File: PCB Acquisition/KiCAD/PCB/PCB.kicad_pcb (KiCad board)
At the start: 2 copper layers, 1 part, among them U1 PIC24F32KA302-I_SS

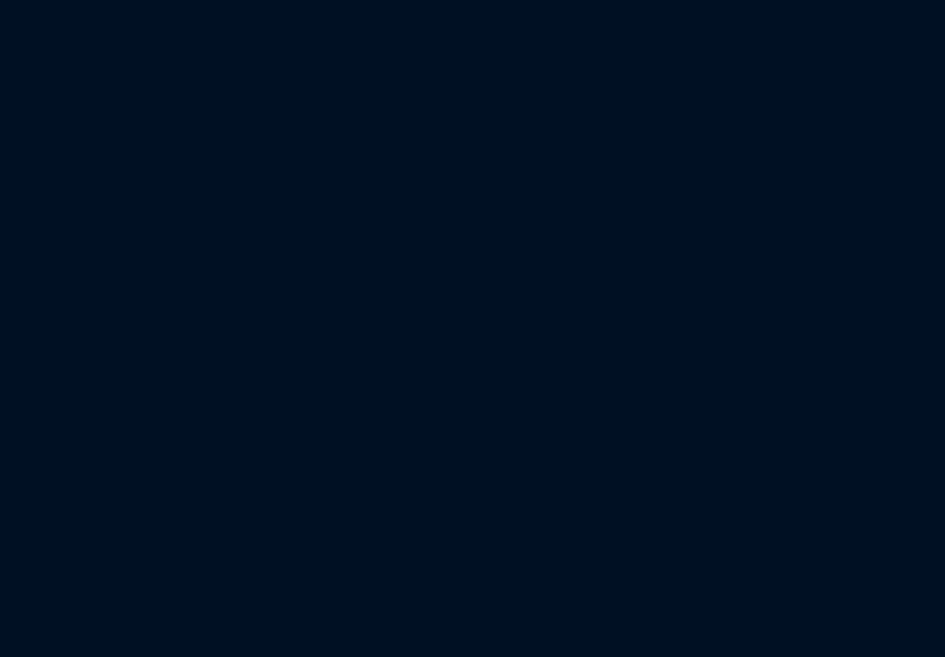
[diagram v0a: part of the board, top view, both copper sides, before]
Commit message: Début du layout
Les pièces ont été choisies pour le PCB et le layout du PCB avec celles-ci est commencé. Il reste à finaliser le layout.
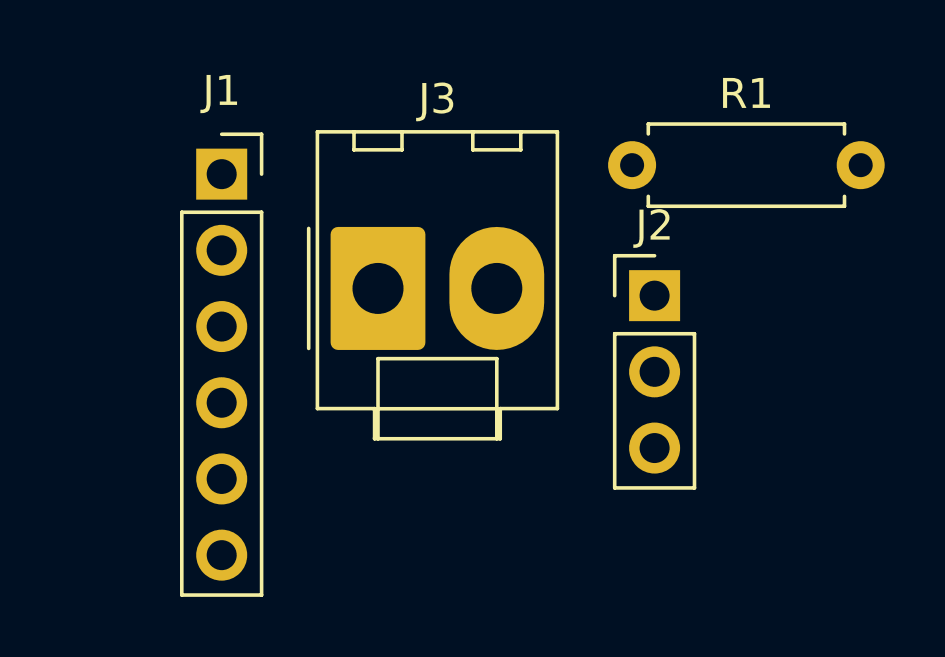
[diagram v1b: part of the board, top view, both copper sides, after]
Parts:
- added J1: Conn_01x06_Female, Connector_PinSocket_2.54mm:PinSocket_1x06_P2.54mm_Vertical, F.Cu at (178.4, 84.4)
- added J2: Conn_01x03_Male, Connector_PinHeader_2.54mm:PinHeader_1x03_P2.54mm_Vertical, F.Cu at (192.8, 88.4)
- added J3: Conn_01x02_Male, Connector_Molex:Molex_KK-396_A-41791-0002_1x02_P3.96mm_Vertical, F.Cu at (183.6, 88.2)
- added R1: 1k, Resistor_THT:R_Axial_DIN0207_L6.3mm_D2.5mm_P7.62mm_Horizontal, F.Cu at (192.0, 84.1)

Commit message: PCB Layout
Layout du PCB
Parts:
- moved J2 45.6 mm to (147.3, 91.4)
- moved J1 41.3 mm to (137.2, 81.3)
- moved R1 41.0 mm to (151.1, 81.5), turned to 180 degrees
- moved J3 7.75 mm to (176.5, 91.4), turned to 90 degrees
- moved U1 2.84 mm to (162.6, 87.6)
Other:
- board outline added: 61 x 25.4 mm
- net class Default: clearance 0.2 -> 0.254; trace_width 0.25 -> 0.254; via_dia 0.8 -> 0.762; via_drill 0.4 -> 0.381
- rule pad_to_mask_clearance: 0.051 -> 0.0508
- rule trace_clearance: 0.2 -> 0.254
- rule trace_min: 0.2 -> 0.1524
- rule via_min_drill: 0.3 -> 0.3302
- rule via_min_size: 0.4 -> 0.6858
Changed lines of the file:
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@@
   (general
     (thickness 1.6)
-    (drawings 0)
+    (drawings 4)
     (tracks 0)
     (zones 0)
@@
   )
   (setup
-    (last_trace_width 0.25)
-    (trace_clearance 0.2)
+    (last_trace_width 0.254)
+    (trace_clearance 0.254)
     (zone_clearance 0.508)
     (zone_45_only no)
-    (trace_min 0.2)
-    (via_size 0.8)
-    (via_drill 0.4)
-    (via_min_size 0.4)
-    (via_min_drill 0.3)
-    (uvia_size 0.3)
-    (uvia_drill 0.1)
+    (trace_min 0.1524)
+    (via_size 0.762)
+    (via_drill 0.381)
+    (via_min_size 0.6858)
+    (via_min_drill 0.3302)
+    (uvia_size 0.762)
+    (uvia_drill 0.381)
     (uvias_allowed no)
-    (uvia_min_size 0.2)
-    (uvia_min_drill 0.1)
+    (uvia_min_size 0.6858)
+    (uvia_min_drill 0.3302)
     (edge_width 0.05)
     (segment_width 0.2)
@@
     (pad_size 1.524 1.524)
     (pad_drill 0.762)
-    (pad_to_mask_clearance 0.051)
+    (pad_to_mask_clearance 0.0508)
     (solder_mask_min_width 0.25)
     (aux_axis_origin 0 0)
@@
   (net 29 "Net-(J3-Pad2)")
   (net_class Default "This is the default net class."
-    (clearance 0.2)
-    (trace_width 0.25)
-    (via_dia 0.8)
-    (via_drill 0.4)
-    (uvia_dia 0.3)
-    (uvia_drill 0.1)
+    (clearance 0.254)
+    (trace_width 0.254)
+    (via_dia 0.762)
+    (via_drill 0.381)
+    (uvia_dia 0.762)
+    (uvia_drill 0.381)
     (add_net "Net-(J1-Pad1)")
     (add_net "Net-(J1-Pad2)")
@@
   )
   (module 24FV32KA302A:PIC24F32KA302-I&slash_SS (layer F.Cu)
-    (at 161.29 90.17)
+    (at 162.56 87.63)
     (fp_text reference U1 (at 0 0) (layer F.SilkS)
       (effects (font (size 1 1) (thickness 0.15)))
@@
   )
   (module Connector_PinSocket_2.54mm:PinSocket_1x06_P2.54mm_Vertical (layer F.Cu)
-    (at 178.355001 84.375001)
+    (at 137.16 81.28)
     (descr "Through hole straight socket strip, 1x06, 2.54mm pitch, single row (from Kicad 4.0.7), script generated")
     (tags "Through hole socket strip THT 1x06 2.54mm single row")
@@
   )
   (module Connector_PinHeader_2.54mm:PinHeader_1x03_P2.54mm_Vertical (layer F.Cu)
-    (at 192.785001 88.425001)
+    (at 147.32 91.44)
     (descr "Through hole straight pin header, 1x03, 2.54mm pitch, single row")
     (tags "Through hole pin header THT 1x03 2.54mm single row")
@@
   )
   (module Connector_Molex:Molex_KK-396_A-41791-0002_1x02_P3.96mm_Vertical (layer F.Cu)
-    (at 183.565001 88.185001)
+    (at 176.53 91.44 90)
     (descr "Molex KK 396 Interconnect System, old/engineering part number: A-41791-0002 example for new part number: 26-60-4020, 2 Pins (https://www.molex.com/pdm_docs/sd/026604020_sd.pdf), generated with kicad-footprint-generator")
     (tags "connector Molex KK-396 vertical")
-    (fp_text reference J3 (at 1.98 -6.31) (layer F.SilkS)
-      (effects (font (size 1 1) (thickness 0.15)))
-    )
-    (fp_text value Conn_01x02_Male (at 1.98 6.1) (layer F.Fab)
+    (fp_text reference J3 (at 1.98 -6.31 90) (layer F.SilkS)
+      (effects (font (size 1 1) (thickness 0.15)))
+    )
+    (fp_text value Conn_01x02_Male (at 1.98 6.1 90) (layer F.Fab)
       (effects (font (size 1 1) (thickness 0.15)))
     )
@@
     (fp_line (start 6.37 5.4) (end 6.37 -5.61) (layer F.CrtYd) (width 0.05))
     (fp_line (start 6.37 -5.61) (end -2.41 -5.61) (layer F.CrtYd) (width 0.05))
-    (fp_text user %R (at 1.98 -4.41) (layer F.Fab)
-      (effects (font (size 1 1) (thickness 0.15)))
-    )
-    (pad 1 thru_hole roundrect (at 0 0) (size 3.16 4.1) (drill 1.7) (layers *.Cu *.Mask) (roundrect_rratio 0.079114)
+    (fp_text user %R (at 1.98 -4.41 90) (layer F.Fab)
+      (effects (font (size 1 1) (thickness 0.15)))
+    )
+    (pad 1 thru_hole roundrect (at 0 0 90) (size 3.16 4.1) (drill 1.7) (layers *.Cu *.Mask) (roundrect_rratio 0.079114)
       (net 28 "Net-(J3-Pad1)"))
-    (pad 2 thru_hole oval (at 3.96 0) (size 3.16 4.1) (drill 1.7) (layers *.Cu *.Mask)
+    (pad 2 thru_hole oval (at 3.96 0 90) (size 3.16 4.1) (drill 1.7) (layers *.Cu *.Mask)
       (net 29 "Net-(J3-Pad2)"))
     (model ${KISYS3DMOD}/Connector_Molex.3dshapes/Molex_KK-396_A-41791-0002_1x02_P3.96mm_Vertical.wrl
@@
   )
   (module Resistor_THT:R_Axial_DIN0207_L6.3mm_D2.5mm_P7.62mm_Horizontal (layer F.Cu)
-    (at 192.035001 84.075001)
+    (at 151.13 81.535001 180)
     (descr "Resistor, Axial_DIN0207 series, Axial, Horizontal, pin pitch=7.62mm, 0.25W = 1/4W, length*diameter=6.3*2.5mm^2, http://cdn-reichelt.de/documents/datenblatt/B400/1_4W%23YAG.pdf")
     (tags "Resistor Axial_DIN0207 series Axial Horizontal pin pitch 7.62mm 0.25W = 1/4W length 6.3mm diameter 2.5mm")
@@
       (effects (font (size 1 1) (thickness 0.15)))
     )
-    (pad 1 thru_hole circle (at 0 0) (size 1.6 1.6) (drill 0.8) (layers *.Cu *.Mask)
+    (pad 1 thru_hole circle (at 0 0 180) (size 1.6 1.6) (drill 0.8) (layers *.Cu *.Mask)
       (net 21 "Net-(J1-Pad1)"))
-    (pad 2 thru_hole oval (at 7.62 0) (size 1.6 1.6) (drill 0.8) (layers *.Cu *.Mask)
+    (pad 2 thru_hole oval (at 7.62 0 180) (size 1.6 1.6) (drill 0.8) (layers *.Cu *.Mask)
       (net 22 "Net-(J1-Pad2)"))
     (model ${KISYS3DMOD}/Resistor_THT.3dshapes/R_Axial_DIN0207_L6.3mm_D2.5mm_P7.62mm_Horizontal.wrl
@@
     )
   )
+  (gr_line (start 127 101.6) (end 187.96 101.6) (layer Edge.Cuts) (width 0.0254))
+  (gr_line (start 187.96 76.2) (end 187.96 101.6) (layer Edge.Cuts) (width 0.0254))
+  (gr_line (start 127 76.2) (end 187.96 76.2) (layer Edge.Cuts) (width 0.0254))
+  (gr_line (start 127 101.6) (end 127 76.2) (layer Edge.Cuts) (width 0.0254))
 )

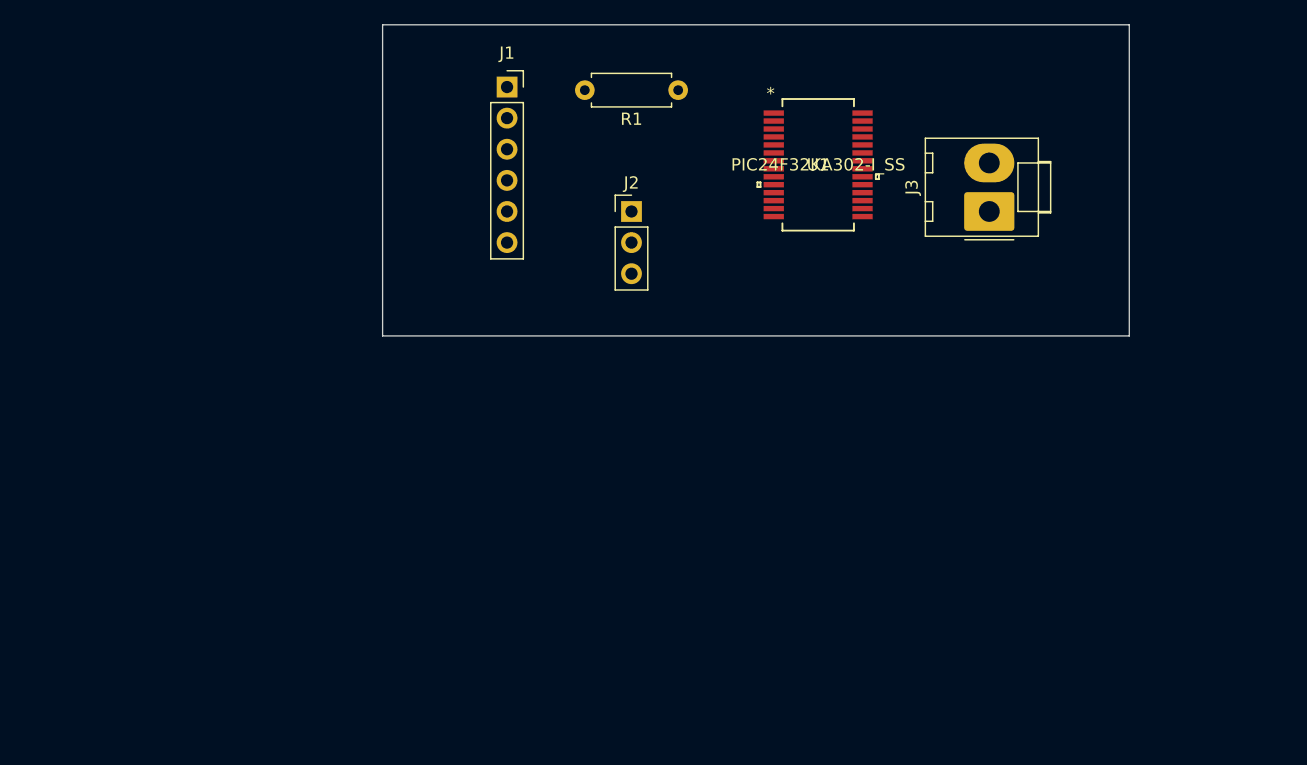
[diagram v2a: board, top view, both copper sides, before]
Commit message: Poursuite du layout (tracks)
Les tracks sont finies.
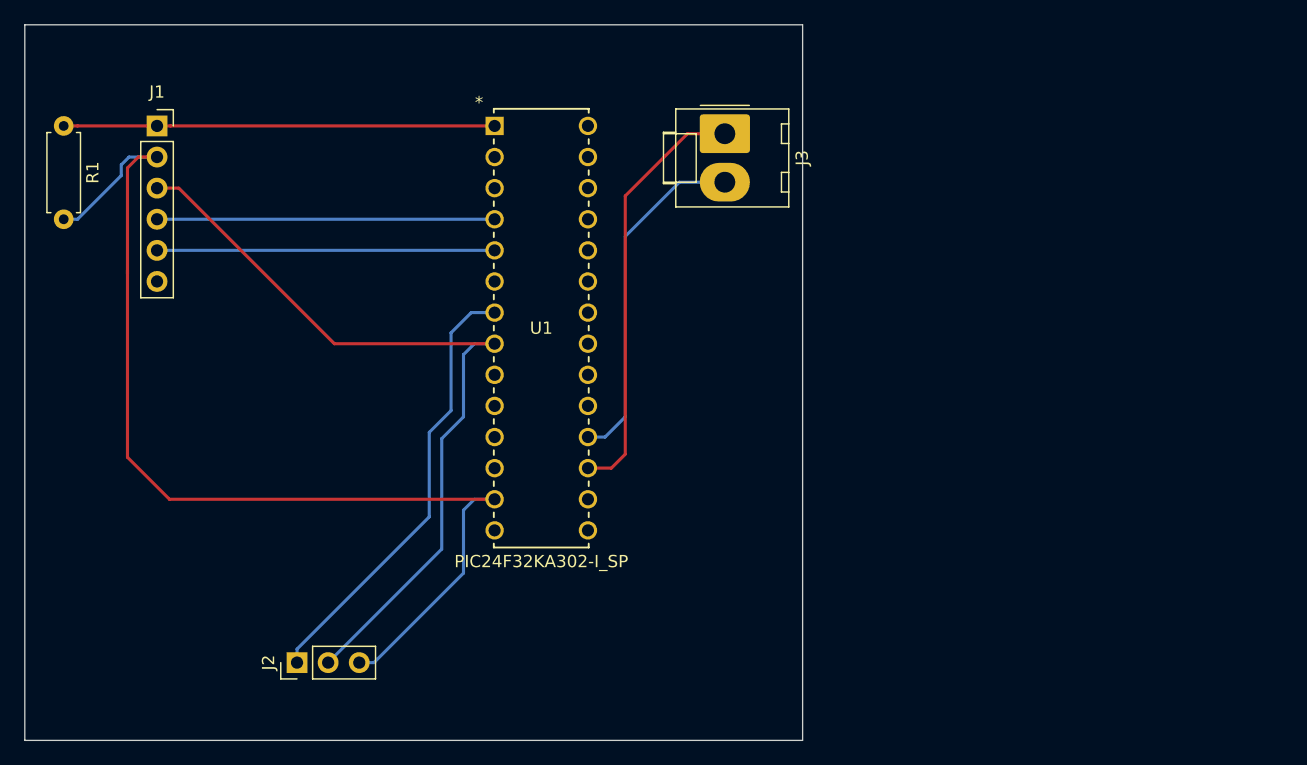
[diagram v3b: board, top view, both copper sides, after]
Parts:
- U1: value PIC24F32KA302-I_SS -> PIC24F32KA302-I_SP; footprint 24FV32KA302A:PIC24F32KA302-I&slash_SS -> PIC24F32KA302:PIC24F32KA302-I&slash_SP
- moved R1 50.2 mm to (101.0, 84.5), turned to 270 degrees
- moved J2 45.8 mm to (120.0, 128.3), turned to 90 degrees
- moved J1 28.8 mm to (108.6, 84.5)
- moved U1 26.6 mm to (136.1, 84.5)
- moved J3 22.5 mm to (154.9, 85.1), turned to 270 degrees
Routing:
- net Net-(J1-Pad2): track 0.00 -> 87.9 mm
- net Net-(J1-Pad3): track 0.00 -> 65.5 mm
- net Net-(J2-Pad1): track 0.00 -> 36.4 mm
- net Net-(J1-Pad1): track 0.00 -> 35.2 mm
- net Net-(J3-Pad1): track 0.00 -> 34.8 mm
- net Net-(J3-Pad2): track 0.00 -> 28.4 mm
- net Net-(J1-Pad5): track 0.00 -> 27.6 mm
- net Net-(J1-Pad4): track 0.00 -> 27.6 mm
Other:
- board size 61 x 25.4 mm -> 63.5 x 58.4 mm

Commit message: PCB fini
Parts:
- removed U1: PIC24F32KA302-I_SP, PIC24F32KA302:PIC24F32KA302-I&slash_SP
- added J4: Conn_01x02_Male, Connector_Molex:Molex_KK-396_A-41791-0002_1x02_P3.96mm_Vertical, F.Cu at (154.9, 97.8)
- J1: value Conn_01x06_Female -> Conn_01x05_Female; footprint Connector_PinSocket_2.54mm:PinSocket_1x06_P2.54mm_Vertical -> Connector_PinSocket_2.54mm:PinSocket_1x05_P2.54mm_Vertical
- J3: value Conn_01x02_Male -> ED281DT; footprint Connector_Molex:Molex_KK-396_A-41791-0002_1x02_P3.96mm_Vertical -> digikey-footprints:Socket_DIP-28_7.62mm_Conn
- moved J3 15.4 mm to (139.6, 84.5), turned to 0 degrees
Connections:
- J3 pad 1: Net-(J3-Pad1) -> Net-(J1-Pad1)
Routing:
- net Net-(J3-Pad1): track 34.8 -> 0.00 mm
- net Net-(J3-Pad2): track 28.4 -> 0.00 mm
- net Net-(J3-Pad18): track 0.00 -> 19.4 mm
- net Net-(J3-Pad17): track 0.00 -> 15.4 mm
- net Net-(J1-Pad2): track 87.9 -> 95.4 mm
- net Net-(J1-Pad3): track 65.5 -> 70.4 mm
- net Net-(J1-Pad5): track 27.6 -> 31.0 mm
- net Net-(J1-Pad4): track 27.6 -> 31.0 mm
- net Net-(J1-Pad1): track 35.2 -> 38.6 mm
- net Net-(J2-Pad1): track 36.4 -> 37.7 mm
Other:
- board text added: "*"
- board text added: "MCLR/Vpp"
- board text added: "PGC"
- board text added: "PGD"
- board text added: "PIC28F32KA302"
- board text added: "PickIt 3"
- board text added: "SCL"
- board text added: "SDA"
- board text added: "SIG"
- board text added: "Vdd"
- board text added: "Vss"
